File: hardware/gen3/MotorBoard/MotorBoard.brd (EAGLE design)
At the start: 140 x 107 mm, 209 parts, among them Q15 2N3904, Q16 IRFZ14, Q23 2N3904, Q24 IRFZ14, Q31 2N3904, Q32 IRFZ14, Q7 IRFZ14, Q8 2N3904, U2 ATMEGA165PV-8AU

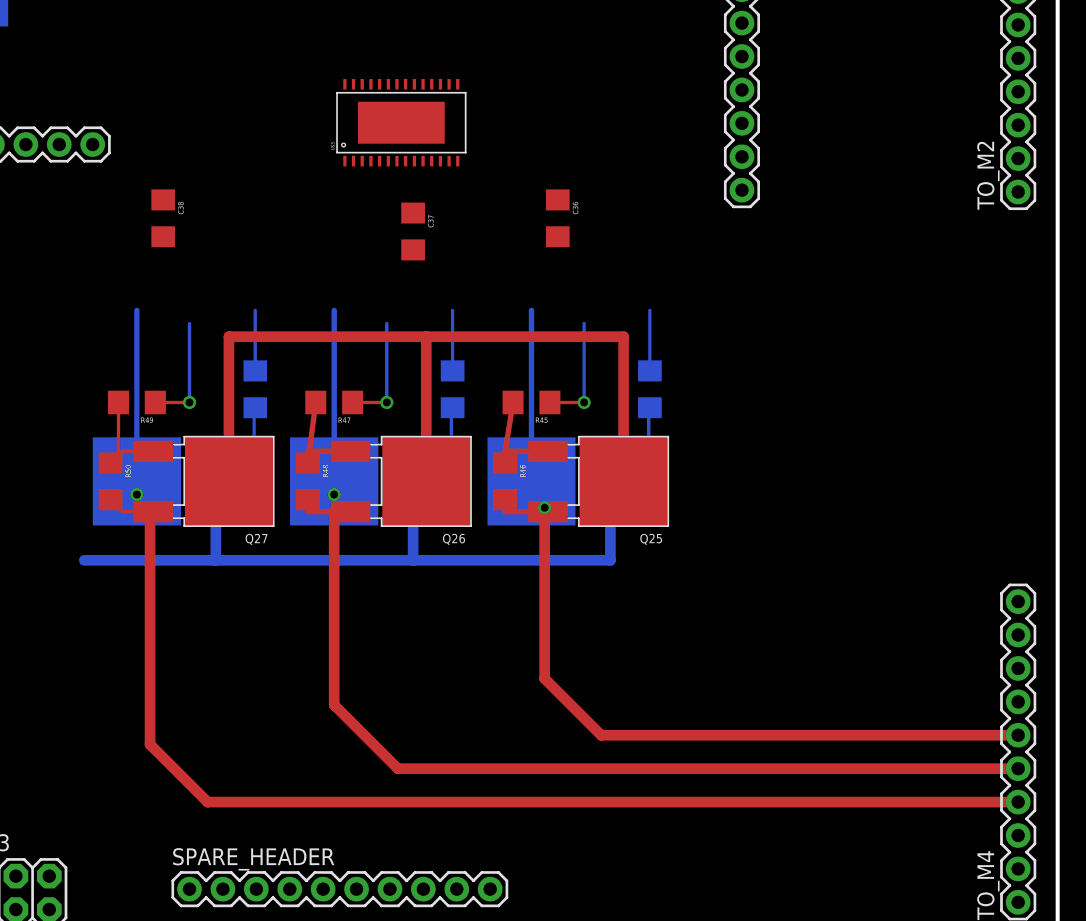
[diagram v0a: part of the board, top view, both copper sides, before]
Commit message: connected one wheel
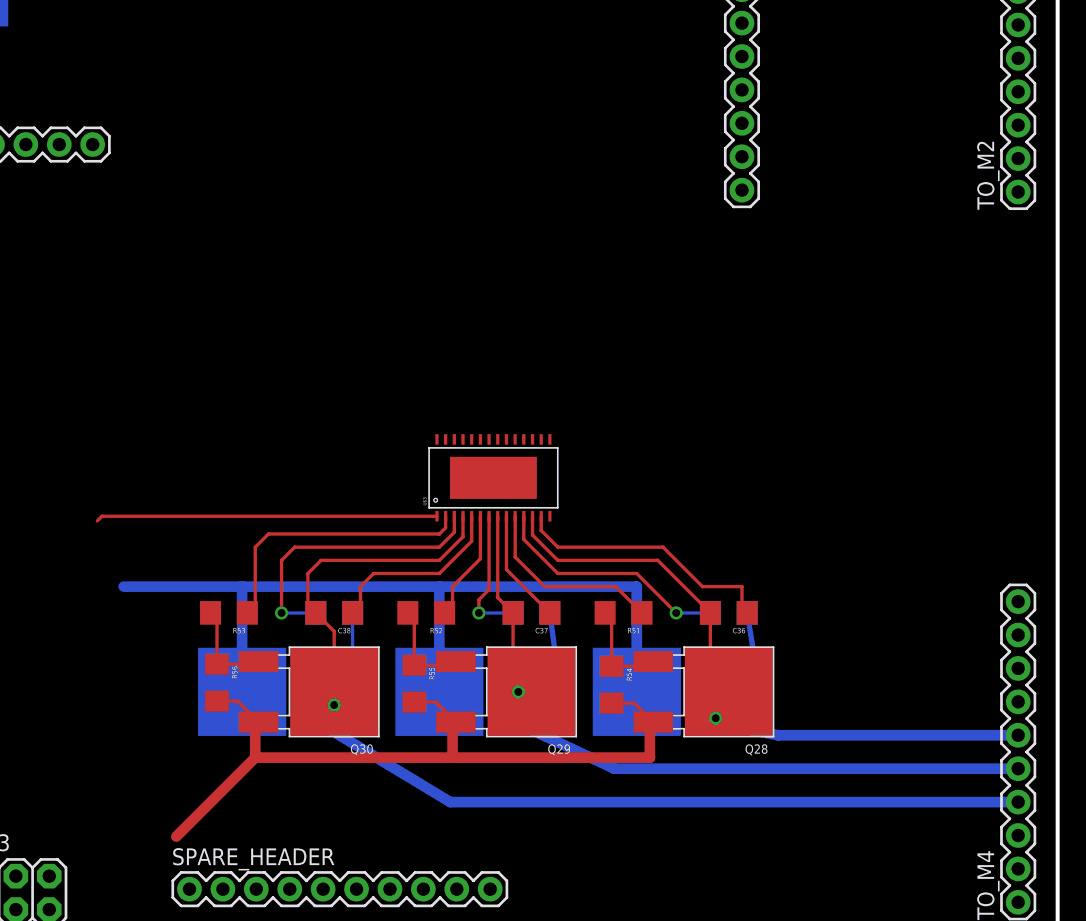
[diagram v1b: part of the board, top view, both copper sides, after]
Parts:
- moved C36 32.7 mm to (115.0, 25.0), turned to 180 degrees
- moved C38 32.7 mm to (85.0, 25.0), turned to 180 degrees
- moved C37 30.4 mm to (100.0, 25.0), turned to 180 degrees
- moved U$3 27.9 mm to (97.1, 35.3)
- moved R46 24.8 mm to (117.0, 19.0), flipped to the bottom
- moved R48 24.8 mm to (102.0, 19.0), flipped to the bottom
- moved R50 24.8 mm to (87.0, 19.0), flipped to the bottom
- moved Q28 21.9 mm to (115.0, 19.0), flipped to the top
- moved Q29 21.9 mm to (100.0, 19.0), flipped to the top
- moved Q30 21.9 mm to (85.0, 19.0), flipped to the top
- moved R45 21.9 mm to (115.0, 25.0), flipped to the bottom
- moved R47 21.9 mm to (100.0, 25.0), flipped to the bottom
- moved R49 21.9 mm to (85.0, 25.0), flipped to the bottom
- moved R51 17.1 mm to (107.0, 25.0), flipped to the top, turned to 180 degrees
- moved R52 17.1 mm to (92.0, 25.0), flipped to the top, turned to 180 degrees
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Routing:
- net M4O2: track 88.2 -> 60.1 mm
- net O4: track 63.4 -> 84.8 mm
- net N$73: track 0.00 -> 20.3 mm
- net M4O3: track 104.5 -> 85.2 mm
- net N$82: track 4.60 -> 21.2 mm
- net M4O1: track 70.6 -> 54.3 mm
- net N$71: track 0.00 -> 14.0 mm
- net N$86: track 8.60 -> 21.8 mm
- net N$84: track 4.60 -> 14.5 mm
- net N$81: track 8.60 -> 18.3 mm
- net N$72: track 0.00 -> 8.72 mm
- net N$83: track 4.60 -> 8.47 mm
- net N$85: track 8.60 -> 10.3 mm
- net N$77: track 8.47 -> 7.62 mm
- net N$79: track 6.94 -> 7.50 mm
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
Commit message: got rid of overcurrent
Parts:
- removed LED10, LED12, LED14, LED16: (no value), SparkFun-LED:LED-1206
- removed Q15, Q23, Q31, Q8: 2N3904, transistor-npn:TO92
- removed Q16, Q24, Q32, Q7: IRFZ14, rfc:DPAK
- removed R100, R102, R104, R98: 130, SparkFun-Passives:1206
- removed R91, R93, R95: 50k, SparkFun-Resistors:1206
- removed R92, R94, R96: 10k, SparkFun-Resistors:1206
- removed RBIG, RBIG1, RBIG2, RBIG3: 100k, SparkFun-Resistors:1206
- added R57, R59, R61: 70k, SparkFun-Resistors:1206
- added R58, R60, R62: 5k, SparkFun-Resistors:1206
- R89: value 50k -> 70k
- R90: value 10k -> 5k
- RSENSE, RSENSE1, RSENSE2, RSENSE3: value .05 -> .02
- moved U$8 146.8 mm to (-96.0, -37.0), flipped to the top
- moved RSENSE3 145.4 mm to (-95.0, -49.0), flipped to the top
- moved U$7 133.5 mm to (-96.0, -20.0), flipped to the top
- moved RSENSE1 131.5 mm to (-95.0, -15.0), flipped to the top
- moved RSENSE2 130.1 mm to (-95.0, -32.0), flipped to the top
- moved U$6 123.7 mm to (-96.0, -3.00), flipped to the top
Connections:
- removed net N$111: R91.1, R92.2, U$6.4
- removed net N$113: R93.1, R94.2, U$7.4
- removed net N$115: R95.1, R96.2, U$8.4
- removed net N$116: LED12.A, R100.1
- removed net N$118: LED14.A, R102.1
- removed net N$120: LED16.A, R104.1
- removed net N$45: Q15.2, Q16.SOURCE, RSENSE1.2, U$6.3
- removed net N$46: Q15.1, Q16.GATE, RBIG1.1
- removed net N$66: Q23.2, Q24.SOURCE, RSENSE2.2, U$8.3
- removed net N$67: Q23.1, Q24.GATE, RBIG2.1
- removed net N$87: Q31.2, Q32.SOURCE, RSENSE3.2, U$7.3
- removed net N$88: Q31.1, Q32.GATE, RBIG3.1
- net 12V: no longer RBIG.2, RBIG1.2, RBIG2.2, RBIG3.2
- net 12VGND: no longer Q15.3, Q23.3, Q31.3, Q8.3
- net 3.3V: no longer U$5.2, U$6.2, U$7.2, U$8.2
- net 5V: now also U$5.2, U$6.2, U$7.2, U$8.2
- net GND: now also R58.1, R60.1, R62.1; no longer LED10.C, LED12.C, LED14.C, LED16.C, R92.1, R94.1, R96.1
- net N$15: now also R59.1, R60.2, U$7.4; no longer Q7.SOURCE, Q8.2, RSENSE.2, U$5.3
- net N$2: now also R57.1, R58.2, U$6.4; no longer LED10.A, R98.1
- net N$22: now also R61.1, R62.2, U$8.4; no longer Q7.GATE, Q8.1, RBIG.1
- net O1: now also RSENSE.2, U$5.3; no longer Q7.DRAIN
- net O2: now also RSENSE1.2, U$6.3; no longer Q16.DRAIN
- net O3: now also RSENSE3.2, U$8.3; no longer Q24.DRAIN
- net O4: now also RSENSE2.2, U$7.3; no longer Q32.DRAIN
- net RLED1: no longer R98.2
- net RLED2: no longer R100.2
- net RLED3: no longer R102.2
- net RLED4: no longer R104.2
- net SENSE1: no longer R91.2, R93.2, R95.2, U$6.1, U$7.1, U$8.1
- net SENSE2: now also R57.2, U$6.1
- net SENSE3: now also R61.2, U$8.1
- net SENSE4: now also R59.2, U$7.1
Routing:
- net O4: track 84.8 -> 0.00 mm

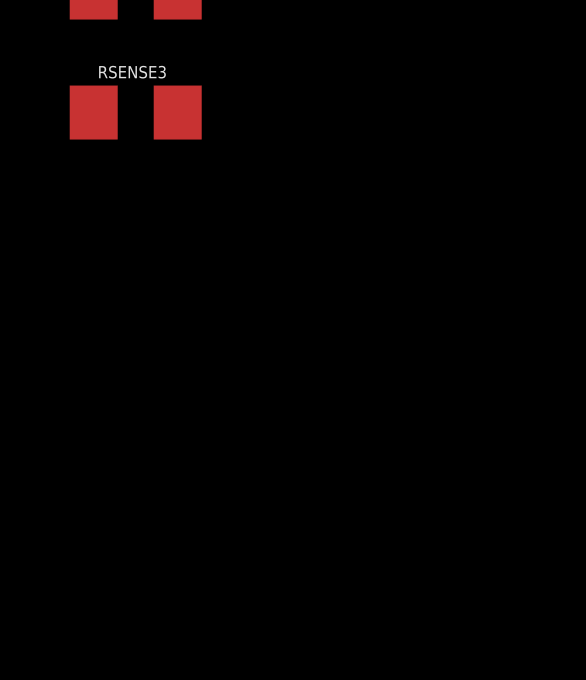
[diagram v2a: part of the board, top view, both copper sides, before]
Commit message: reading in fault pins
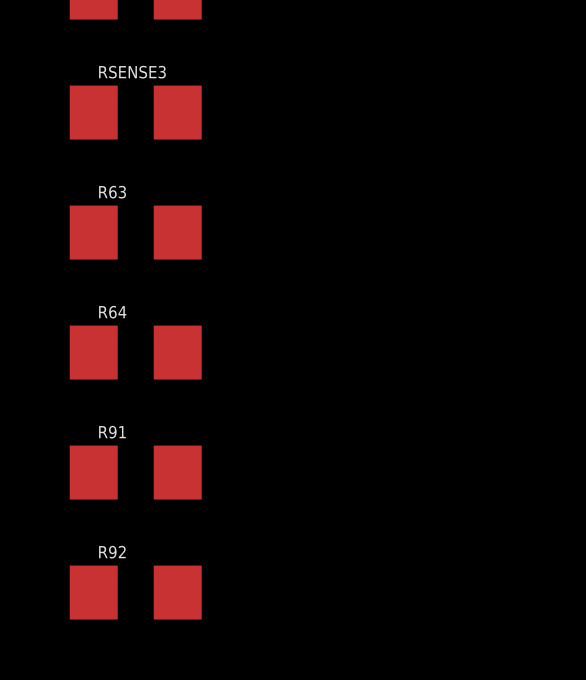
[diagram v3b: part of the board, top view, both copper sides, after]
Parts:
- added R63, R64, R91, R92: 1k, SparkFun-Resistors:1206
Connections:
- new net FAULT1: R63.1, U$4.FAULT, U2.33
- new net FAULT2: R64.1, U$1.FAULT, U2.34
- new net FAULT3: R91.1, U$2.FAULT, U2.43
- new net FAULT4: R92.1, U$3.FAULT, U2.18
- net 3.3V: now also R63.2, R64.2, R91.2, R92.2; no longer U$1.FAULT, U$2.FAULT, U$3.FAULT, U$4.FAULT
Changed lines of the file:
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@@
 <element name="R61" library="SparkFun-Resistors" package="1206" value="70k" x="-95" y="-41"/>
 <element name="R62" library="SparkFun-Resistors" package="1206" value="5k" x="-95" y="-45"/>
+<element name="R63" library="SparkFun-Resistors" package="1206" value="1k" x="-95" y="-53"/>
+<element name="R64" library="SparkFun-Resistors" package="1206" value="1k" x="-95" y="-57"/>
+<element name="R91" library="SparkFun-Resistors" package="1206" value="1k" x="-95" y="-61"/>
+<element name="R92" library="SparkFun-Resistors" package="1206" value="1k" x="-95" y="-65"/>
 </elements>
 <signals>
@@
 <contactref element="LOGIC_HEADER" pad="3"/>
 <contactref element="LOGIC_HEADER" pad="4"/>
-<contactref element="U$4" pad="FAULT"/>
-<contactref element="U$4" pad="VDD"/>
 <contactref element="U$4" pad="SPEED"/>
 <contactref element="C6" pad="2"/>
 <contactref element="U$2" pad="SPEED"/>
 <contactref element="C24" pad="2"/>
-<contactref element="U$2" pad="FAULT"/>
 <contactref element="U$2" pad="VDD"/>
 <contactref element="U$3" pad="SPEED"/>
 <contactref element="U$3" pad="VDD"/>
 <contactref element="C15" pad="2"/>
-<contactref element="U$3" pad="FAULT"/>
 <contactref element="C39" pad="2"/>
-<contactref element="U$1" pad="FAULT"/>
-<contactref element="U$1" pad="VDD"/>
 <contactref element="U$1" pad="SPEED"/>
 <contactref element="R97" pad="2"/>
 <contactref element="U2" pad="21"/>
 <contactref element="U2" pad="52"/>
+<contactref element="U$4" pad="VDD"/>
+<contactref element="R63" pad="2"/>
+<contactref element="U$1" pad="VDD"/>
+<contactref element="R64" pad="2"/>
+<contactref element="R91" pad="2"/>
+<contactref element="R92" pad="2"/>
 <wire x1="67.206" y1="85.38" x2="73.6068" y2="100.62" width="0" layer="19" extent="1-1"/>
 <wire x1="24" y1="64.62" x2="67.206" y2="85.38" width="0" layer="19" extent="1-1"/>
@@
 <wire x1="6.54" y1="34.66" x2="5.41" y2="52.71" width="0" layer="19" extent="16-16"/>
 <wire x1="16.34" y1="33.66" x2="6.54" y2="34.66" width="0" layer="19" extent="16-16"/>
-<wire x1="4.189" y1="7.2254" x2="6.54" y2="34.66" width="0" layer="19" extent="16-16"/>
-<wire x1="4.183" y1="6.565" x2="4.189" y2="7.2254" width="0" layer="19" extent="16-16"/>
+<wire x1="4.183" y1="6.565" x2="6.54" y2="34.66" width="0" layer="19" extent="16-16"/>
 <wire x1="4.189" y1="5.2442" x2="4.183" y2="6.565" width="0" layer="19" extent="16-16"/>
-<wire x1="1.569" y1="6.2254" x2="4.183" y2="6.565" width="0" layer="19" extent="16-16"/>
-<wire x1="1.563" y1="5.565" x2="1.569" y2="6.2254" width="0" layer="19" extent="16-16"/>
+<wire x1="1.563" y1="5.565" x2="4.189" y2="5.2442" width="0" layer="19" extent="16-16"/>
 <wire x1="1.569" y1="4.2442" x2="1.563" y2="5.565" width="0" layer="19" extent="16-16"/>
 <wire x1="13.423" y1="5.565" x2="4.189" y2="5.2442" width="0" layer="19" extent="16-16"/>
-<wire x1="13.429" y1="6.2254" x2="13.423" y2="5.565" width="0" layer="19" extent="16-16"/>
 <wire x1="13.429" y1="4.2442" x2="13.423" y2="5.565" width="0" layer="19" extent="16-16"/>
 <wire x1="58.26" y1="4.99" x2="13.423" y2="5.565" width="0" layer="19" extent="16-16"/>
-<wire x1="96.7746" y1="38.191" x2="58.26" y2="4.99" width="0" layer="19" extent="1-1"/>
-<wire x1="97.435" y1="38.197" x2="96.7746" y2="38.191" width="0" layer="19" extent="1-1"/>
+<wire x1="97.435" y1="38.197" x2="58.26" y2="4.99" width="0" layer="19" extent="1-1"/>
 <wire x1="98.7558" y1="38.191" x2="97.435" y2="38.197" width="0" layer="19" extent="1-1"/>
+<wire x1="-93.6" y1="-53" x2="1.569" y2="4.2442" width="0" layer="19" extent="1-16"/>
+<wire x1="-93.6" y1="-57" x2="-93.6" y2="-53" width="0" layer="19" extent="1-1"/>
+<wire x1="-93.6" y1="-61" x2="-93.6" y2="-57" width="0" layer="19" extent="1-1"/>
+<wire x1="-93.6" y1="-65" x2="-93.6" y2="-61" width="0" layer="19" extent="1-1"/>
 </signal>
 <signal name="MOSI">
@@
 <wire x1="50.69" y1="77.13" x2="16.02" y2="41.28" width="0" layer="19" extent="16-16"/>
 </signal>
+<signal name="FAULT1">
+<contactref element="U2" pad="33"/>
+<contactref element="U$4" pad="FAULT"/>
+<contactref element="R63" pad="1"/>
+<wire x1="13.429" y1="6.2254" x2="77.62" y2="87.0056" width="0" layer="19" extent="1-16"/>
+<wire x1="-96.4" y1="-53" x2="13.429" y2="6.2254" width="0" layer="19" extent="1-16"/>
+</signal>
+<signal name="FAULT2">
+<contactref element="U2" pad="34"/>
+<contactref element="U$1" pad="FAULT"/>
+<contactref element="R64" pad="1"/>
+<wire x1="1.569" y1="6.2254" x2="77.62" y2="87.793" width="0" layer="19" extent="1-16"/>
+<wire x1="-96.4" y1="-57" x2="1.569" y2="6.2254" width="0" layer="19" extent="1-16"/>
+</signal>
+<signal name="FAULT3">
+<contactref element="U2" pad="43"/>
+<contactref element="U$2" pad="FAULT"/>
+<contactref element="R91" pad="1"/>
+<wire x1="4.189" y1="7.2254" x2="77.62" y2="95.0066" width="0" layer="19" extent="1-16"/>
+<wire x1="-96.4" y1="-61" x2="4.189" y2="7.2254" width="0" layer="19" extent="1-16"/>
+</signal>
+<signal name="FAULT4">
+<contactref element="U2" pad="18"/>
+<contactref element="R92" pad="1"/>
+<contactref element="U$3" pad="FAULT"/>
+<wire x1="96.7746" y1="38.191" x2="-96.4" y2="-65" width="0" layer="19" extent="1-1"/>
+<wire x1="64.793" y1="85.38" x2="96.7746" y2="38.191" width="0" layer="19" extent="1-1"/>
+</signal>
 </signals>

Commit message: hooked up ss lines
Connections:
- net SS2 renamed SS_K
- net SS3 renamed SS_E1
- net SS4 renamed SS_E2
- net SS5 renamed SS_E3
- removed net RLED1: U2.36
- removed net RLED2: U2.38
- removed net RLED3: U2.40
- removed net RLED4: U2.42
- removed net SS1: SPI_HEADER.4
- new net SS_M: SPI_HEADER.4, U2.11
- net 12VGND: now also D1.A, D2.A
- net GLED2: now also U2.36; no longer U2.37
- net GLED3: now also U2.37; no longer U2.39
- net GLED4: now also U2.38; no longer U2.41
- net SCK: no longer U2.11
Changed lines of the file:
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@@
 <contactref element="LED15" pad="C"/>
 <contactref element="U$6" pad="5"/>
-<contactref element="R58" pad="1"/>
 <contactref element="U$7" pad="5"/>
 <contactref element="R60" pad="1"/>
 <contactref element="U$8" pad="5"/>
 <contactref element="R62" pad="1"/>
+<contactref element="R58" pad="1"/>
 <wire x1="137" y1="25.86" x2="137" y2="79.86" width="0" layer="19" extent="1-1"/>
 <wire x1="100.0766" y1="38.191" x2="137" y2="25.86" width="0" layer="19" extent="1-1"/>
@@
 <contactref element="R4" pad="1"/>
 <contactref element="JP13" pad="3"/>
-<contactref element="U2" pad="11"/>
-<wire x1="3.4" y1="52.71" x2="62.38" y2="90.9934" width="0" layer="19" extent="1-16"/>
-<wire x1="60.8" y1="2.45" x2="3.4" y2="52.71" width="0" layer="19" extent="16-16"/>
-</signal>
-<signal name="SS1">
-<contactref element="SPI_HEADER" pad="4"/>
-</signal>
-<signal name="SS2">
+<wire x1="3.4" y1="52.71" x2="60.8" y2="2.45" width="0" layer="19" extent="16-16"/>
+</signal>
+<signal name="SS_K">
 <contactref element="SPI_HEADER" pad="5"/>
 </signal>
-<signal name="SS3">
+<signal name="SS_E1">
 <contactref element="SPI_HEADER" pad="6"/>
 </signal>
-<signal name="SS4">
+<signal name="SS_E2">
 <contactref element="SPI_HEADER" pad="7"/>
 </signal>
-<signal name="SS5">
+<signal name="SS_E3">
 <contactref element="SPI_HEADER" pad="8"/>
 </signal>
@@
 <contactref element="RSENSE2" pad="1"/>
 <contactref element="RSENSE3" pad="1"/>
+<contactref element="D2" pad="A"/>
+<contactref element="D1" pad="A"/>
 <wire x1="-96.4" y1="-32" x2="-96.4" y2="-49" width="0" layer="19" extent="1-1"/>
 <wire x1="-96.4" y1="-15" x2="-96.4" y2="-32" width="0" layer="19" extent="1-1"/>
@@
 <wire x1="9.54" y1="54.71" x2="5.49" y2="53.71" width="0" layer="19" extent="16-16"/>
 <wire x1="11.84" y1="53.71" x2="9.54" y2="54.71" width="0" layer="19" extent="16-16"/>
+<wire x1="11.87" y1="53.71" x2="11.84" y2="53.71" width="0" layer="19" extent="16-16"/>
 <wire x1="12.79" y1="52.71" x2="11.84" y2="53.71" width="0" layer="19" extent="16-16"/>
 <wire x1="14.1" y1="52.71" x2="12.79" y2="52.71" width="0" layer="19" extent="16-16"/>
-<wire x1="15.89" y1="54.71" x2="14.1" y2="52.71" width="0" layer="19" extent="16-16"/>
+<wire x1="15.68" y1="53.71" x2="14.1" y2="52.71" width="0" layer="19" extent="16-16"/>
+<wire x1="15.89" y1="54.71" x2="15.68" y2="53.71" width="0" layer="19" extent="16-16"/>
 <wire x1="18.19" y1="53.71" x2="15.89" y2="54.71" width="0" layer="19" extent="16-16"/>
 <wire x1="19.14" y1="52.71" x2="18.19" y2="53.71" width="0" layer="19" extent="16-16"/>
@@
 </signal>
 <signal name="GLED1">
+<contactref element="R1" pad="2"/>
 <contactref element="U2" pad="35"/>
-<contactref element="R1" pad="2"/>
 <wire x1="1.42" y1="34.66" x2="77.62" y2="88.6058" width="0" layer="19" extent="1-16"/>
 </signal>
-<signal name="RLED1">
+<signal name="GLED2">
+<contactref element="R99" pad="2"/>
 <contactref element="U2" pad="36"/>
-</signal>
-<signal name="GLED2">
+<wire x1="11.26" y1="48.9" x2="77.62" y2="89.3932" width="0" layer="19" extent="1-16"/>
+</signal>
+<signal name="GLED3">
+<contactref element="R101" pad="2"/>
 <contactref element="U2" pad="37"/>
-<contactref element="R99" pad="2"/>
-<wire x1="11.26" y1="48.9" x2="77.62" y2="90.206" width="0" layer="19" extent="1-16"/>
-</signal>
-<signal name="RLED2">
+<wire x1="1.42" y1="49.9" x2="77.62" y2="90.206" width="0" layer="19" extent="1-16"/>
+</signal>
+<signal name="GLED4">
+<contactref element="R103" pad="2"/>
 <contactref element="U2" pad="38"/>
-</signal>
-<signal name="GLED3">
-<contactref element="U2" pad="39"/>
-<contactref element="R101" pad="2"/>
-<wire x1="1.42" y1="49.9" x2="77.62" y2="91.8062" width="0" layer="19" extent="1-16"/>
-</signal>
-<signal name="RLED3">
-<contactref element="U2" pad="40"/>
-</signal>
-<signal name="GLED4">
-<contactref element="U2" pad="41"/>
-<contactref element="R103" pad="2"/>
-<wire x1="11.58" y1="49.9" x2="77.62" y2="93.4064" width="0" layer="19" extent="1-16"/>
-</signal>
-<signal name="RLED4">
-<contactref element="U2" pad="42"/>
+<wire x1="11.58" y1="49.9" x2="77.62" y2="90.9934" width="0" layer="19" extent="1-16"/>
 </signal>
 <signal name="N$97">
@@
 <wire x1="64.793" y1="85.38" x2="96.7746" y2="38.191" width="0" layer="19" extent="1-1"/>
 </signal>
+<signal name="SS_M">
+<contactref element="U2" pad="11"/>
+<contactref element="SPI_HEADER" pad="4"/>
+<wire x1="62.38" y1="90.9934" x2="116" y2="72.38" width="0" layer="19" extent="1-1"/>
+</signal>
 </signals>
